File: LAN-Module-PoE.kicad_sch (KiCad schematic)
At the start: 91 parts, among them J10 ProtoCastellatedHeader, J11 ProtoCastellatedHeader, J12 ProtoCastellatedHeader, J13 ProtoCastellatedHeader, J14 ProtoCastellatedHeader, J15 ProtoCastellatedHeader, J16 ProtoCastellatedHeader, J17 ProtoCastellatedHeader, J18 ProtoCastellatedHeader, J19 ProtoCastellatedHeader, J20 ProtoCastellatedHeader, J21 ProtoCastellatedHeader, J22 ProtoCastellatedHeader, J23 ProtoCastellatedHeader, J24 ProtoCastellatedHeader, J25 ProtoCastellatedHeader, J26 ProtoCastellatedHeader, J27 ProtoCastellatedHeader, J28 ProtoCastellatedHeader, J3 ProtoCastellatedHeader, J4 ProtoCastellatedHeader, J5 ProtoCastellatedHeader, J6 ProtoCastellatedHeader, J7 ProtoCastellatedHeader, J8 ProtoCastellatedHeader, J9 ProtoCastellatedHeader, SW1 RESET, U1 ESP32-U4WDH, U4 RTL8201F, Y1 40MHz ±10ppm

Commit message: Final revision of PoE variant
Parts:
- added C17: 100n, Capacitor_SMD:C_0603_1608Metric, symbol EspGateway-rescue:C_Small-device-EspGateway-rescue
- added D3: (no value), symbol Device:LED_Small_Filled
- added R26: 33k 1%, Resistor_SMD:R_0603_1608Metric, symbol EspGateway-rescue:R_Small_US-device-EspGateway-rescue
- added R27: 10k 1%, Resistor_SMD:R_0603_1608Metric, symbol EspGateway-rescue:R_Small_US-device-EspGateway-rescue
- added R28: (no value), Resistor_SMD:R_0603_1608Metric, symbol EspGateway-rescue:R_Small_US-device-EspGateway-rescue
- C1: value (none) -> 100n
- C18: value (none) -> 2.2u; footprint (none) -> Capacitor_SMD:C_0805_2012Metric
- C21, C4: value (none) -> 1u; footprint (none) -> Capacitor_SMD:C_0603_1608Metric
- C27: value (none) -> 10u; footprint (none) -> Capacitor_SMD:C_Elec_6.3x5.4
- C6: value (none) -> 1nF
- D1: value (none) -> SL310A; footprint (none) -> Diode_SMD:D_SMA
- D2: value (none) -> PMEG6020ER,115; footprint (none) -> Diode_SMD:D_SOD-123
- J1: value (none) -> HY931147C; footprint (none) -> Connector_RJ:RJ45_Wuerth_7499111446_Horizontal
- L2: value (none) -> 10uH 1A; footprint (none) -> Inductor_SMD:L_Taiyo-Yuden_NR-40xx
- L4: value (none) -> 10uH; footprint (none) -> Inductor_SMD:L_Taiyo-Yuden_NR-60xx
- R19: value (none) -> 0R
- R20: value (none) -> 620m
- R21: value (none) -> 47k
- R6: value (none) -> 24.3k 1%
- R7: value (none) -> 48.7R; footprint (none) -> Resistor_SMD:R_0603_1608Metric
- U2: value (none) -> Si3404; footprint (none) -> Package_DFN_QFN:QFN-20-1EP_4x4mm_P0.5mm_EP2.6x2.6mm
- U3: value (none) -> LV2842XLVDDCR; footprint (none) -> Package_TO_SOT_SMD:SOT-23-6
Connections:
- net 3V3 is gone; now on net +3V3: J15.1
- net VIN is gone; now on net 12V: C1.1, C18.1, C27.1, C4.1, D1.1 (K), J1.9 (V+), J28.1, R19.1, R23.2, R6.1, U2.13 (VPOS)
- net +3V3: now also L2.2, D3.2 (A), R26.2
- net GND: now also D2.2 (A), J1.SH (SHIELD), R27.1, R28.1
- net at L2.1: now also D2.1 (K), U3.6 (SW), C17.2
- net at U3.1 (CB): now also C17.1
- net at U3.3 (FB): now also R26.1, R27.2
- net 12V: now reaches U3.4 (~{SHDN})
- net 12V: now also U3.5 (VIN)
- new net: D3.1 (K), R28.2
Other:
- note added: "3.3V REG"
- note added: "Ceramic caps should be X5R or X7R Diode should be fast recovery type f_sw = 550kHz"
- note added: "Imax = 600mA"
- note added: "VOUT = 0.765V(1+(R1/R2)) R1 = R2 * ((VOUT/0.765)-1)"
- note added: "WARNING: PoE is referenced to +V, so GND is -12V with respect to PoE voltage"
- note removed: "TODO: 3.3V REG"
- moved on the sheet: C21, D2, L2

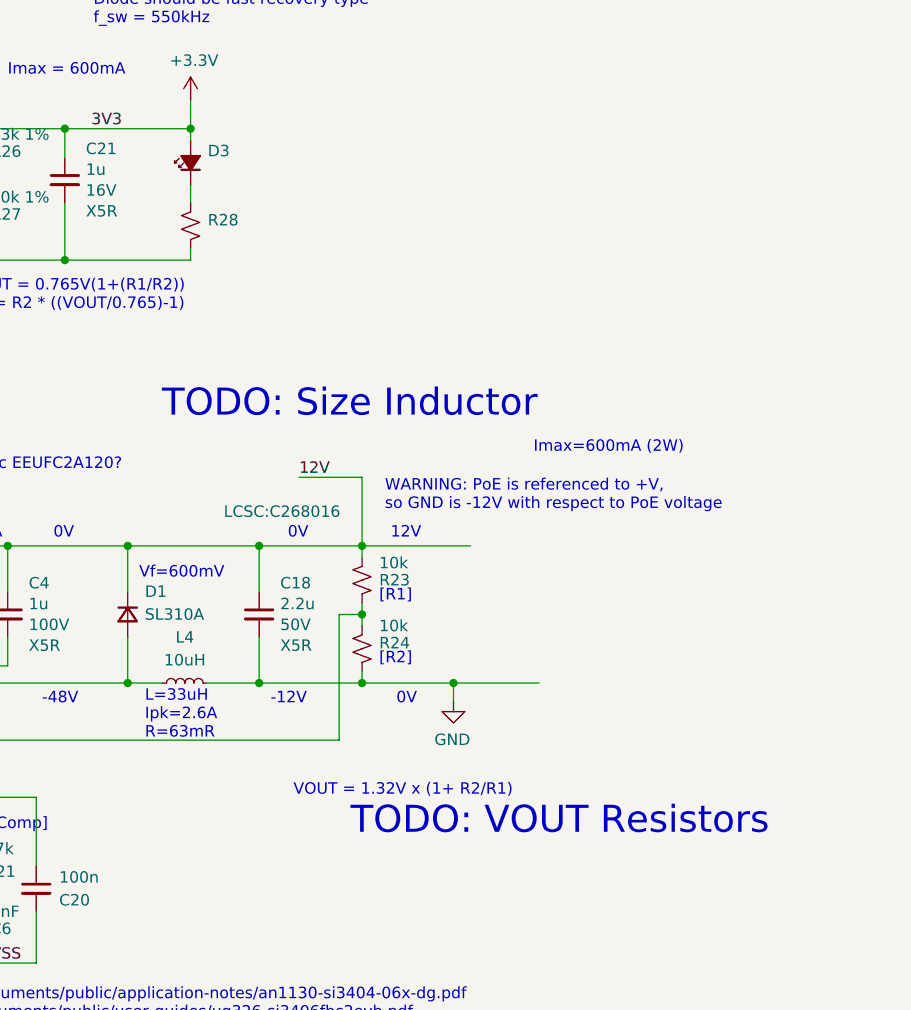
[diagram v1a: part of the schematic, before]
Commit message: Fix footprint for ESP32 (QFN 5x5), add heat pad for PoE regulator
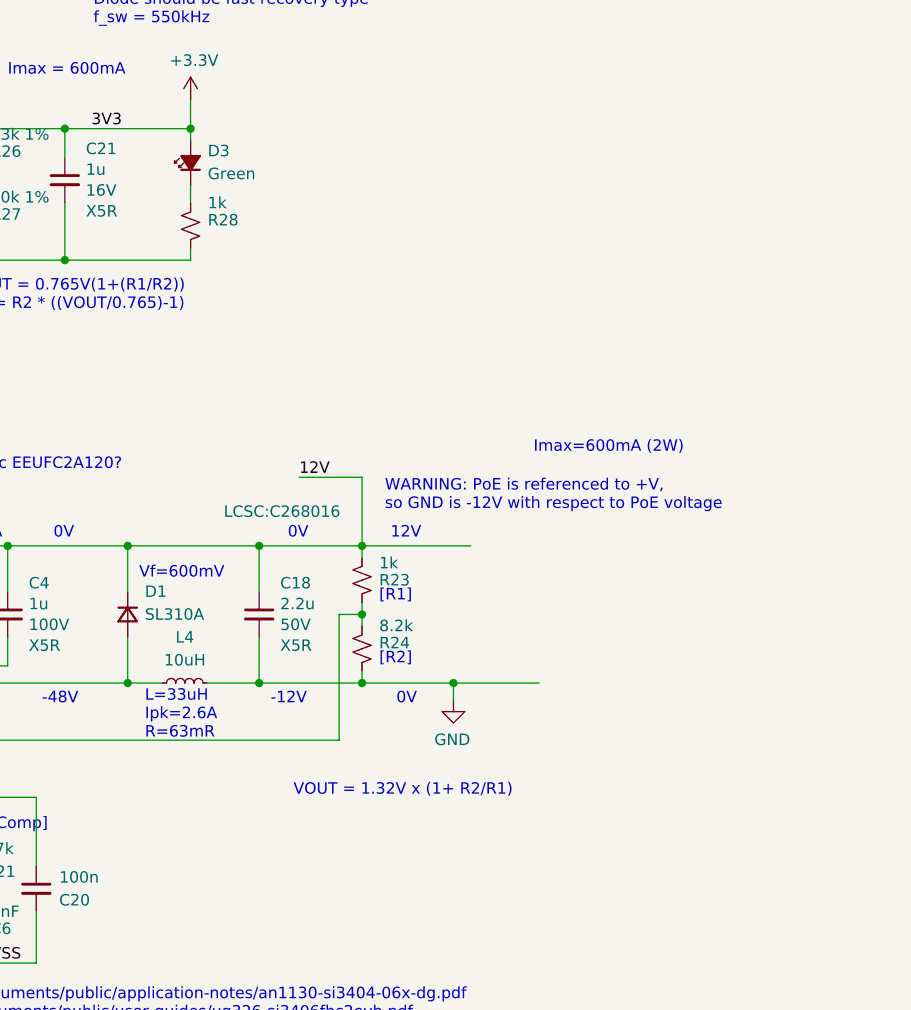
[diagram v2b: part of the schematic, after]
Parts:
- D3: value (none) -> Green; footprint (none) -> LED_SMD:LED_0603_1608Metric
- R23: value 10k -> 1k
- R24: value 10k -> 8.2k
- R28: value (none) -> 1k
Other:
- note removed: "TODO: Size Inductor"
- note removed: "TODO: VOUT Resistors"
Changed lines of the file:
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@@
     (effects (font (size 1.27 1.27)) (justify left bottom))
   )
-  (text "TODO: VOUT Resistors" (at 359.41 121.92 0)
-    (effects (font (size 3 3)) (justify left bottom))
-  )
-  (text "TODO: Size Inductor" (at 338.455 75.565 0)
-    (effects (font (size 3 3)) (justify left bottom))
-  )
   (text "AUX POWER" (at 382.27 223.52 0)
     (effects (font (size 1.27 1.27)) (justify left bottom))
@@
       (effects (font (size 1.27 1.27)) (justify left))
     )
-    (property "Value" "10k" (id 1) (at 362.585 98.425 0)
+    (property "Value" "8.2k" (id 1) (at 362.585 98.425 0)
       (effects (font (size 1.27 1.27)) (justify left))
     )
@@
       (effects (font (size 1.27 1.27)) (justify left))
     )
-    (property "Value" "" (id 1) (at 343.535 51.435 0)
+    (property "Value" "1k" (id 1) (at 343.535 51.435 0)
       (effects (font (size 1.27 1.27)) (justify left))
     )
@@
       (effects (font (size 1.27 1.27)) (justify left))
     )
-    (property "Value" "10k" (id 1) (at 362.585 91.44 0)
+    (property "Value" "1k" (id 1) (at 362.585 91.44 0)
       (effects (font (size 1.27 1.27)) (justify left))
     )
@@
       (effects (font (size 1.27 1.27)) (justify right))
     )
-    (property "Value" "" (id 1) (at 343.535 48.1964 90)
+    (property "Value" "Green" (id 1) (at 343.535 48.1964 90)
       (effects (font (size 1.27 1.27)) (justify right))
     )
-    (property "Footprint" "" (id 2) (at 341.63 46.99 90)
+    (property "Footprint" "LED_SMD:LED_0603_1608Metric" (id 2) (at 341.63 46.99 90)
       (effects (font (size 1.27 1.27)) hide)
     )
@@
     )
     (path "/539964a4-2da9-4e75-8b3c-85fdccc5578e"
-      (reference "R23") (unit 1) (value "10k") (footprint "Resistor_SMD:R_0603_1608Metric")
+      (reference "R23") (unit 1) (value "1k") (footprint "Resistor_SMD:R_0603_1608Metric")
     )
     (path "/47adf5bf-6373-4545-94fc-af4ee3a07475"
-      (reference "R24") (unit 1) (value "10k") (footprint "Resistor_SMD:R_0603_1608Metric")
+      (reference "R24") (unit 1) (value "8.2k") (footprint "Resistor_SMD:R_0603_1608Metric")
     )
     (path "/e22df168-6afe-4fad-b3b4-74c1ef18090b"

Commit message: Finalize layout for rev2
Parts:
- added C28: 1u, Capacitor_SMD:C_0603_1608Metric, symbol EspGateway-rescue:C_Small-device-EspGateway-rescue
- added J2, J29: ProtoCastellatedHeader, Visclib:ProtoHeader_65mil, symbol Visclib:ProtoCastellatedHeader
- added R29, R30, R31, R32: 50R, Resistor_SMD:R_0603_1608Metric, symbol EspGateway-rescue:R_Small_US-device-EspGateway-rescue
- added TP1, TP2: TP, Visclib:TP-1MM, symbol visclib:TP
- C1, C21: Dielectric X5R -> (none); Spec (none) -> X5R
- C10, C11, C14, C5: Range (none) -> 3.3V
- C17: Dielectric X5R -> (none); Range (none) -> 12V; Spec (none) -> X5R
- C20: Range (none) -> 5V
- C22: footprint Capacitor_SMD:C_0603_1608Metric -> Resistor_SMD:R_0603_1608Metric; Spec (none) -> X5R
- C23, C24, C25, C26: Spec (none) -> X5R
- C3: Dielectric Y5V -> (none); Range (none) -> 50V; Rating 50V -> (none); Spec (none) -> Y5V
- C7: value 100n -> 1u; Dielectric (none) -> X5R; Range (none) -> 100V; now left out of the parts list
- C8: footprint Capacitor_SMD:C_0603_1608Metric -> Resistor_SMD:R_0603_1608Metric
- J10, J11, J12, J13, J14, J15, J16, J17, J18, J19, J20, J21, J22, J23, J24, J25, J26, J27, J28, J3, J4, J5, J6, J7, J8, J9: footprint Visclib:ProtoCastellatedHeader_65mil -> Visclib:ProtoHeader_65mil
- L4: value 10uH -> 33uH
- R13: Spec (none) -> 1%
- R14, R17, R18: value 49.9R 1% -> 50R 1%; Spec (none) -> 1%
- R20: value 620m -> 1.2R; footprint Resistor_SMD:R_0603_1608Metric -> Resistor_SMD:R_0805_2012Metric; Spec (none) -> 1/10W
- R7: value 48.7R -> 75R
- U1: footprint Visclib:ESP32-REDUCED -> Package_DFN_QFN:QFN-48-1EP_5x5mm_P0.35mm_EP3.7x3.7mm_ThermalVias
- Y1: value 40MHz ±10ppm -> 40MHz; Spec (none) -> ±10ppm
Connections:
- net +3V3: no longer C7.2
- net 12V: now also C7.1, C28.1, J2.1
- net ETH_CLK: now also R32.1; no longer U4.32 (CKXTAL2)
- net ETH_CRS_DV: now also R31.1; no longer U4.26 (CRS_DV)
- net ETH_RST: now also TP1.1
- net ETH_RXD0: now also R29.1; no longer U4.9 (RXD0)
- net ETH_RXD1: now also R30.1; no longer U4.10 (RXD1)
- net GND: no longer C7.1
- net VIN_NEG: now also J29.1
- net VSS: now also C7.2, C28.2
- net at C20.1, U2.5 (VDD): now also TP2.1
- new net: R32.2, U4.32 (CKXTAL2)
- new net CRS_DV: R31.2, U4.26 (CRS_DV)
- new net RXD0: R29.2, U4.9 (RXD0)
- new net RXD1: R30.2, U4.10 (RXD1)
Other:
- note added: "Integrated TVS Diode"
- note added: "Length match within 50mm (not important in this design)"
- note added: "NOTE: Chip reaches 85C-110C with 12W load, depending on part selection"
- note added: "NOTE: Ripple 5V pk-pk for L=10uH !!"
- note added: "NOTE: Type 2 / Class 4 / 20W not supported for Si3404."
- note added: "OPT"
- note added: "PSRAM must be disabled as we need GPIO17 for CLKOUT"
- note added: "R SMD footprint for trace layout"
- note added: "Series termination resistors required on TX from PHY and CLK for stability"
- note added: "[CDet]"
- note removed: "AUX POWER"
- note removed: "TODO"
- moved on the sheet: C1, C18, C20, C27, C4, C6, D1, L4, R19, R20, R21, R23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

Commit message: Final PoE design with fixes for rev2 gerber spin
- MTDI must not be pulled high
- GPIO17 for PHY clock conflicts with internal flash
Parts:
- removed R5: 10K, Resistor_SMD:R_0603_1608Metric, symbol EspGateway-rescue:R_Small_US-device-EspGateway-rescue
- removed TP2: TP, Visclib:TP-1MM, symbol visclib:TP
- added C29: 2.2u, Capacitor_SMD:C_0805_2012Metric, symbol EspGateway-rescue:C_Small-device-EspGateway-rescue
- added L5: -, Inductor_SMD:L_Taiyo-Yuden_NR-60xx, symbol Device:L_Small
- C4: footprint Capacitor_SMD:C_0603_1608Metric -> Capacitor_SMD:C_0805_2012Metric
- L4: footprint Inductor_SMD:L_Taiyo-Yuden_NR-60xx -> Inductor_SMD:L_Taiyo-Yuden_NR-80xx_HandSoldering
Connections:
- net 12V: now also C29.1
- net BOOT: now also R32.1
- net GND: now also C29.2, L5.2
- net SWO: now also L5.1
- net ETHCLK: now reaches R32.2, U4.32 (CKXTAL2)
- net ETH_CLK: no longer names the net of U1.27 (GPIO17)
- net ETH_CLK: no longer R32.1
- no-connect marks 16 -> 17
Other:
- note added: "3.3V"
- note added: "FLASH_CS"
- note added: "FLASH_DO"
- note added: "For chips with int. flash, MTDI must be pulled !!low!! (U4WDH, 3.3V SDIO)"
- note added: "GPIO16/17 is used for internal flash"
- note removed: "1.8V"
- note removed: "For chips with int. flash, MTDI must be pulled high (U4WDH)"
- note removed: "PSRAM must be disabled as we need GPIO17 for CLKOUT"
- moved on the sheet: R23, R24

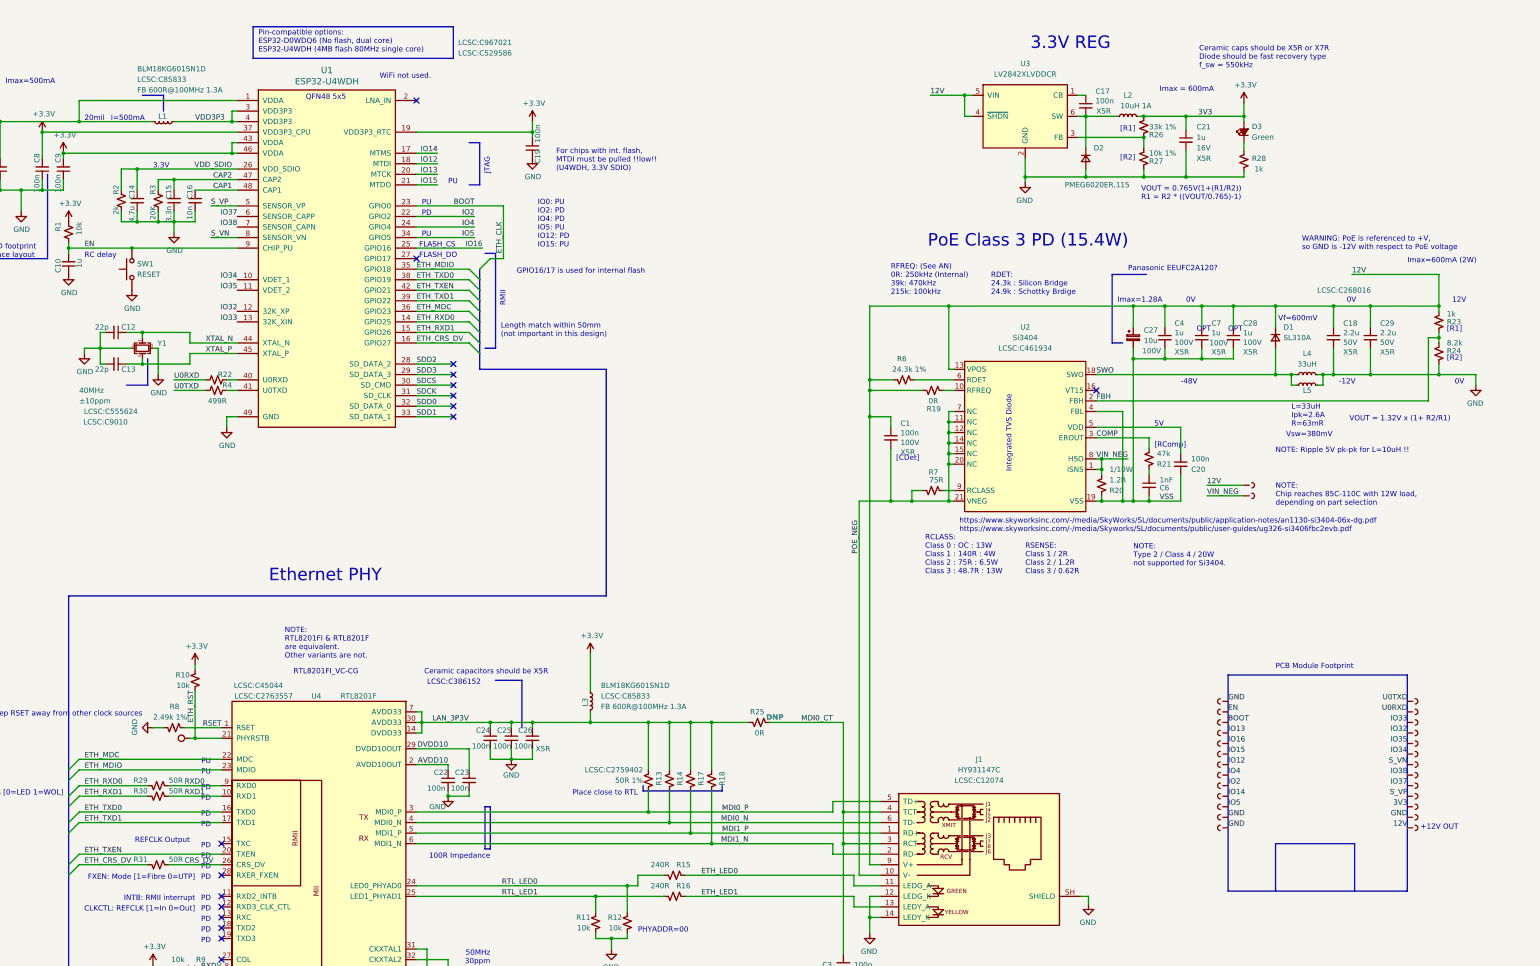
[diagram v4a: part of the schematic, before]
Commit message: Update LCSC part numbers and adjust component values to available parts
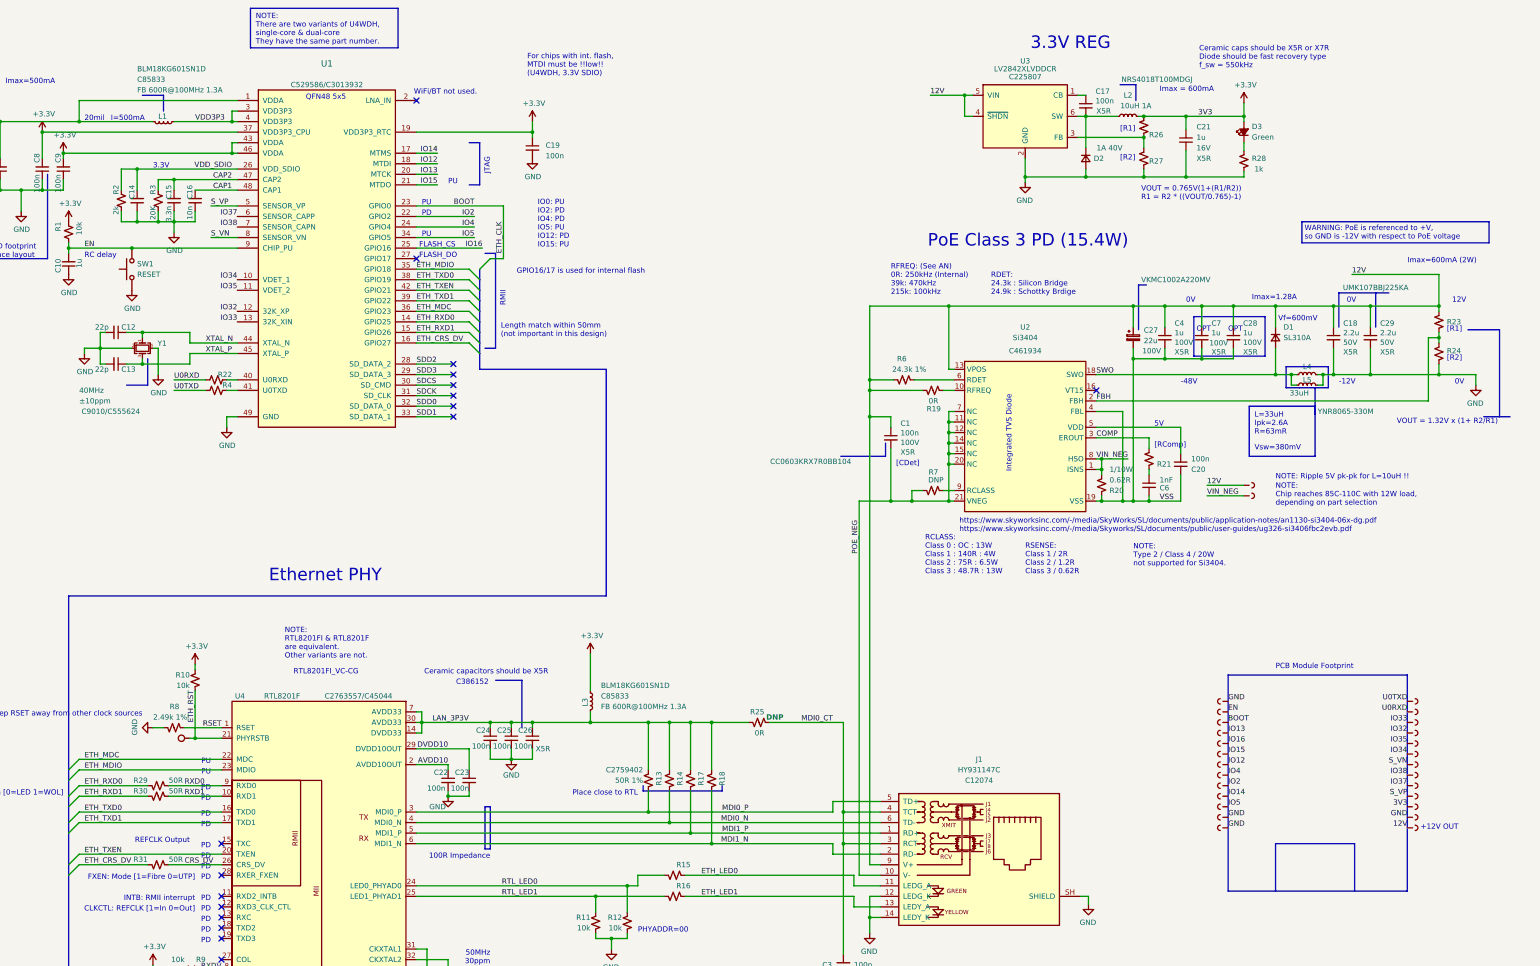
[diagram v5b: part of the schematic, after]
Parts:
- C1: LCSC (none) -> C113803; Part (none) -> CC0603KRX7R0BB104
- C14: value 4.7u -> (none)
- C18, C29: LCSC (none) -> C268016; Part (none) -> UMK107BBJ225KA; Part1 LCSC:C268016 -> (none)
- C27: value 10u -> 22u; LCSC (none) -> C487431; Part (none) -> VKMC1002A220MV
- C4: LCSC (none) -> C385977; Part (none) -> HMK212BC7105KGHTE
- D2: value PMEG6020ER,115 -> (none); footprint Diode_SMD:D_SOD-123 -> (none); LCSC (none) -> C2685454; Rating (none) -> 1A 40V
- J1: LCSC (none) -> C12074; Part LCSC:C12074 -> (none)
- L1, L3: LCSC (none) -> C85833; MfrPart BLM18KG601SN1D -> (none); Part (none) -> BLM18KG601SN1D; Part1 LCSC:C85833 -> (none)
- L2: LCSC (none) -> C222882; Part (none) -> NRS4018T100MDGJ
- L4: LCSC (none) -> C2681905; Part (none) -> YNR8065-330M; Rating (none) -> 1.2A
- R13: LCSC (none) -> C2759402; Part LCSC:C2759402 -> (none); Spec 1% -> (none); Tolerance (none) -> 1%
- R14, R17: Spec 1% -> (none); Tolerance (none) -> 1%
- R15, R16: value 240R -> (none)
- R18: Spec 1% -> Tolerance
- R20: value 1.2R -> 0.62R; LCSC (none) -> C2930222
- R21: value 47k -> (none)
- R22, R4: value 499R -> (none); footprint Resistor_SMD:R_0603_1608Metric -> (none)
- R23: value 1k -> (none); footprint Resistor_SMD:R_0603_1608Metric -> (none); LCSC (none) -> C22548
- R24: value 8.2k -> (none); footprint Resistor_SMD:R_0603_1608Metric -> (none); LCSC (none) -> C114637
- R26: value 33k 1% -> (none); footprint Resistor_SMD:R_0603_1608Metric -> (none); LCSC (none) -> C126359
- R27: value 10k 1% -> (none); footprint Resistor_SMD:R_0603_1608Metric -> (none); LCSC (none) -> C98220
- R6: LCSC (none) -> C2930079
- R7: value 75R -> DNP
- R8: LCSC (none) -> C2930072
- U1: value ESP32-U4WDH -> (none); footprint Package_DFN_QFN:QFN-48-1EP_5x5mm_P0.35mm_EP3.7x3.7mm_ThermalVias -> (none); LCSC (none) -> C529586/C3013932; Part1 LCSC:C529586 -> (none); Part2 LCSC:C967021 -> (none)
- U2: LCSC (none) -> C461934; Part LCSC:C461934 -> (none)
- U3: LCSC (none) -> C225807
- U4: LCSC (none) -> C2763557/C45044; Part1 LCSC:C2763557 -> (none); Part2 LCSC:C45044 -> (none)
- Y1: LCSC (none) -> C9010/C555624; Part1 LCSC:C9010 -> (none); Part2 LCSC:C555624 -> (none)
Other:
- note added: "C386152"
- note added: "For chips with int. flash, MTDI must be !!low!! (U4WDH, 3.3V SDIO)"
- note added: "NOTE: There are two variants of U4WDH, single-core & dual-core They have the same part number."
- note added: "WiFi/BT not used."
- note removed: "For chips with int. flash, MTDI must be pulled !!low!! (U4WDH, 3.3V SDIO)"
- note removed: "LCSC:C386152"
- note removed: "Panasonic EEUFC2A120?"
- note removed: "Pin-compatible options: ESP32-D0WDQ6 (No flash, dual core) ESP32-U4WDH (4MB flash 80MHz single core)"
- note removed: "WiFi not used."
